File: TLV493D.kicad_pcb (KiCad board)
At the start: 2 copper layers, 11.7 x 22.6 mm, 10 parts, among them J1 Conn_01x04_Female, U1 TLV493D

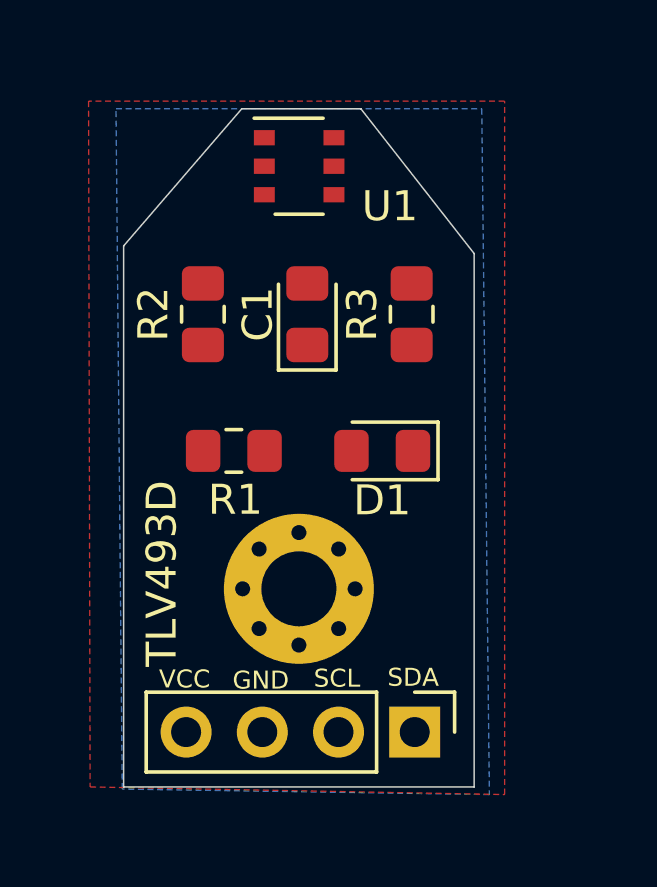
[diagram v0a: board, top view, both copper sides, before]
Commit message: Corrections routeo
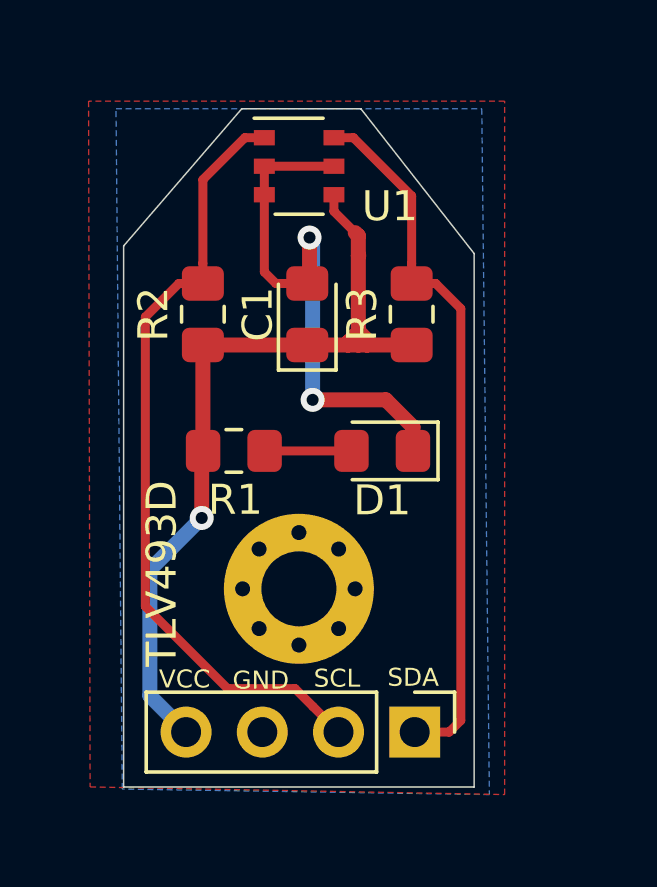
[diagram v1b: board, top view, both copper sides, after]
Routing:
- net VCC: track 0.00 -> 31.0 mm, vias 0 -> 1
- net /SCL: track 0.00 -> 26.3 mm
- net /SDA: track 0.00 -> 23.7 mm
- net GND: track 0.00 -> 19.0 mm, vias 0 -> 2
- net Net-(D1-Pad2): track 0.00 -> 2.90 mm
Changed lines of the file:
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@@
-(kicad_pcb (version 20171130) (host pcbnew "(5.1.4-0-10_14)")
+(kicad_pcb (version 20171130) (host pcbnew "(5.1.4)-1")
   (general
     (thickness 1.6)
     (drawings 15)
-    (tracks 0)
+    (tracks 61)
     (zones 0)
     (modules 10)
@@
     (34 B.Paste user)
     (35 F.Paste user)
-    (36 B.SilkS user)
+    (36 B.SilkS user hide)
     (37 F.SilkS user)
     (38 B.Mask user)
@@
   (gr_line (start 155.99 98.044) (end 159.766 102.87) (layer Edge.Cuts) (width 0.05))
   (gr_line (start 152.02 98.044) (end 155.99 98.044) (layer Edge.Cuts) (width 0.05))
+  (segment (start 152.7724 100.9092) (end 152.7724 103.4837) (width 0.3) (layer F.Cu) (net 1))
+  (segment (start 153.1567 103.868) (end 154.2034 103.868) (width 0.3) (layer F.Cu) (net 1))
+  (segment (start 152.7724 103.4837) (end 153.1567 103.868) (width 0.3) (layer F.Cu) (net 1))
+  (segment (start 152.7724 99.9592) (end 152.7724 100.9092) (width 0.3) (layer F.Cu) (net 1))
+  (segment (start 152.7724 99.9592) (end 155.0924 99.9592) (width 0.3) (layer F.Cu) (net 1))
+  (via (at 154.3812 107.7468) (size 0.8) (drill 0.4) (layers F.Cu B.Cu) (net 1))
+  (segment (start 156.8248 107.7468) (end 154.3812 107.7468) (width 0.5) (layer F.Cu) (net 1))
+  (segment (start 157.7266 109.4486) (end 157.7266 108.6486) (width 0.5) (layer F.Cu) (net 1))
+  (segment (start 157.7266 108.6486) (end 156.8248 107.7468) (width 0.5) (layer F.Cu) (net 1))
+  (via (at 154.2796 102.3366) (size 0.8) (drill 0.4) (layers F.Cu B.Cu) (net 1))
+  (segment (start 154.3812 107.7468) (end 154.3812 102.4382) (width 0.5) (layer B.Cu) (net 1))
+  (segment (start 154.3812 102.4382) (end 154.2796 102.3366) (width 0.5) (layer B.Cu) (net 1))
+  (segment (start 154.2796 103.7918) (end 154.2034 103.868) (width 0.5) (layer F.Cu) (net 1))
+  (segment (start 154.2796 102.3366) (end 154.2796 103.7918) (width 0.5) (layer F.Cu) (net 1))
+  (segment (start 150.7236 109.4412) (end 150.731 109.4486) (width 0.5) (layer F.Cu) (net 2))
+  (segment (start 150.7236 105.918) (end 150.7236 109.4412) (width 0.5) (layer F.Cu) (net 2))
+  (segment (start 150.7236 105.918) (end 154.2034 105.918) (width 0.5) (layer F.Cu) (net 2))
+  (segment (start 156.1973 105.918) (end 157.6832 105.918) (width 0.5) (layer F.Cu) (net 2))
+  (segment (start 154.2034 105.918) (end 155.5623 105.918) (width 0.5) (layer F.Cu) (net 2))
+  (segment (start 155.0924 100.9092) (end 155.0924 101.4642) (width 0.3) (layer F.Cu) (net 2))
+  (segment (start 155.5623 105.8291) (end 155.9198 105.4716) (width 0.5) (layer F.Cu) (net 2))
+  (segment (start 155.5623 105.918) (end 155.5623 105.8291) (width 0.5) (layer F.Cu) (net 2))
+  (segment (start 156.1973 105.7491) (end 155.9198 105.4716) (width 0.5) (layer F.Cu) (net 2))
+  (segment (start 156.1973 105.918) (end 156.1973 105.7491) (width 0.5) (layer F.Cu) (net 2))
+  (segment (start 155.9052 102.95) (end 155.9198 102.9354) (width 0.5) (layer F.Cu) (net 2))
+  (segment (start 155.9052 105.918) (end 155.9052 102.95) (width 0.5) (layer F.Cu) (net 2))
+  (segment (start 155.9198 102.2916) (end 155.9198 102.9354) (width 0.3) (layer F.Cu) (net 2))
+  (segment (start 155.9198 102.9354) (end 155.9198 105.4716) (width 0.3) (layer F.Cu) (net 2))
+  (segment (start 155.9052 105.918) (end 156.1973 105.918) (width 0.5) (layer F.Cu) (net 2))
+  (segment (start 155.5623 105.918) (end 155.9052 105.918) (width 0.5) (layer F.Cu) (net 2))
+  (segment (start 155.9052 102.277) (end 155.80165 102.17345) (width 0.5) (layer F.Cu) (net 2))
+  (segment (start 155.9052 102.95) (end 155.9052 102.277) (width 0.5) (layer F.Cu) (net 2))
+  (segment (start 155.0924 101.4642) (end 155.80165 102.17345) (width 0.3) (layer F.Cu) (net 2))
+  (segment (start 155.80165 102.17345) (end 155.9198 102.2916) (width 0.3) (layer F.Cu) (net 2))
+  (via (at 150.6855 111.6838) (size 0.8) (drill 0.4) (layers F.Cu B.Cu) (net 2))
+  (segment (start 150.6855 109.4941) (end 150.731 109.4486) (width 0.5) (layer F.Cu) (net 2))
+  (segment (start 150.6855 111.6838) (end 150.6855 109.4941) (width 0.5) (layer F.Cu) (net 2))
+  (segment (start 148.957 117.6134) (end 150.1648 118.8212) (width 0.5) (layer B.Cu) (net 2))
+  (segment (start 150.6855 111.6838) (end 148.957 113.4123) (width 0.5) (layer B.Cu) (net 2))
+  (segment (start 148.957 113.4123) (end 148.957 117.6134) (width 0.5) (layer B.Cu) (net 2))
+  (segment (start 152.781 109.4486) (end 155.6766 109.4486) (width 0.3) (layer F.Cu) (net 3))
+  (segment (start 150.7236 103.193) (end 150.7236 103.868) (width 0.3) (layer F.Cu) (net 4))
+  (segment (start 150.7236 100.408) (end 150.7236 103.193) (width 0.3) (layer F.Cu) (net 4))
+  (segment (start 152.1224 99.0092) (end 150.7236 100.408) (width 0.3) (layer F.Cu) (net 4))
+  (segment (start 152.7724 99.0092) (end 152.1224 99.0092) (width 0.3) (layer F.Cu) (net 4))
+  (segment (start 149.9236 103.868) (end 148.8059 104.9857) (width 0.3) (layer F.Cu) (net 4))
+  (segment (start 150.7236 103.868) (end 149.9236 103.868) (width 0.3) (layer F.Cu) (net 4))
+  (segment (start 148.8059 104.9857) (end 148.8059 114.6302) (width 0.3) (layer F.Cu) (net 4))
+  (segment (start 154.394801 117.971201) (end 155.2448 118.8212) (width 0.3) (layer F.Cu) (net 4))
+  (segment (start 153.794799 117.371199) (end 154.394801 117.971201) (width 0.3) (layer F.Cu) (net 4))
+  (segment (start 151.546899 117.371199) (end 153.794799 117.371199) (width 0.3) (layer F.Cu) (net 4))
+  (segment (start 148.8059 114.6302) (end 151.546899 117.371199) (width 0.3) (layer F.Cu) (net 4))
+  (segment (start 157.6832 103.193) (end 157.6832 103.868) (width 0.3) (layer F.Cu) (net 5))
+  (segment (start 157.6832 100.95) (end 157.6832 103.193) (width 0.3) (layer F.Cu) (net 5))
+  (segment (start 155.7424 99.0092) (end 157.6832 100.95) (width 0.3) (layer F.Cu) (net 5))
+  (segment (start 155.0924 99.0092) (end 155.7424 99.0092) (width 0.3) (layer F.Cu) (net 5))
+  (segment (start 158.9348 118.8212) (end 157.7848 118.8212) (width 0.3) (layer F.Cu) (net 5))
+  (segment (start 159.3215 118.4345) (end 158.9348 118.8212) (width 0.3) (layer F.Cu) (net 5))
+  (segment (start 159.3215 104.7063) (end 159.3215 118.4345) (width 0.3) (layer F.Cu) (net 5))
+  (segment (start 158.4832 103.868) (end 159.3215 104.7063) (width 0.3) (layer F.Cu) (net 5))
+  (segment (start 157.6832 103.868) (end 158.4832 103.868) (width 0.3) (layer F.Cu) (net 5))
   (zone (net 1) (net_name GND) (layer F.Cu) (hatch edge 0.508)
     (connect_pads (clearance 0.508))

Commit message: new sizes
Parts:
- added G***: LOGO, Aesthetics:SCL, F.Cu at (156.2, 116.2)
- added G***: LOGO, Aesthetics:3v3, F.Cu at (151.1, 116.1)
- added G***: LOGO, Aesthetics:GND, F.Cu at (153.7, 116.1)
- added G***: LOGO, Aesthetics:SDA, F.Cu at (158.8, 116.2)
- added G***: LOGO, Aesthetics:SDA, B.Cu at (158.8, 116.2)
- added G***: LOGO, Aesthetics:GND, B.Cu at (153.7, 116.5)
- added G***: LOGO, Aesthetics:3v3, B.Cu at (151.3, 116.2)
- added G***: LOGO, Aesthetics:SCL, B.Cu at (156.1, 116.2)
- moved D1 3.67 mm to (159.7, 111.5), turned to 270 degrees
- moved R1 2.86 mm to (150.6, 112.1), turned to 90 degrees
- moved REF** 2.55 mm to (155.0, 111.8)
- moved R3 1.96 mm to (159.6, 105.3)
- moved REF** 1.71 mm to (155.0, 106.5)
- moved G*** 1.18 mm to (155.1, 100.7)
- moved U1 1.12 mm to (155.1, 99.9)
- moved J1 1.02 mm to (158.8, 118.8)
- moved C1 0.91 mm to (155.0, 105.3)
- moved R2 0.58 mm to (150.7, 105.5)
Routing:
- net VCC: track 31.0 -> 0.00 mm, vias 1 -> 0
- net /SCL: track 26.3 -> 0.00 mm
- net /SDA: track 23.7 -> 0.00 mm
- net GND: track 19.0 -> 0.00 mm, vias 2 -> 0
- net Net-(D1-Pad2): track 2.90 -> 0.00 mm
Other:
- board size 11.7 x 22.6 mm -> 14 x 22.6 mm
- board text removed: "GND"
- board text removed: "SCL"
- board text removed: "SDA"
- board text removed: "VCC"

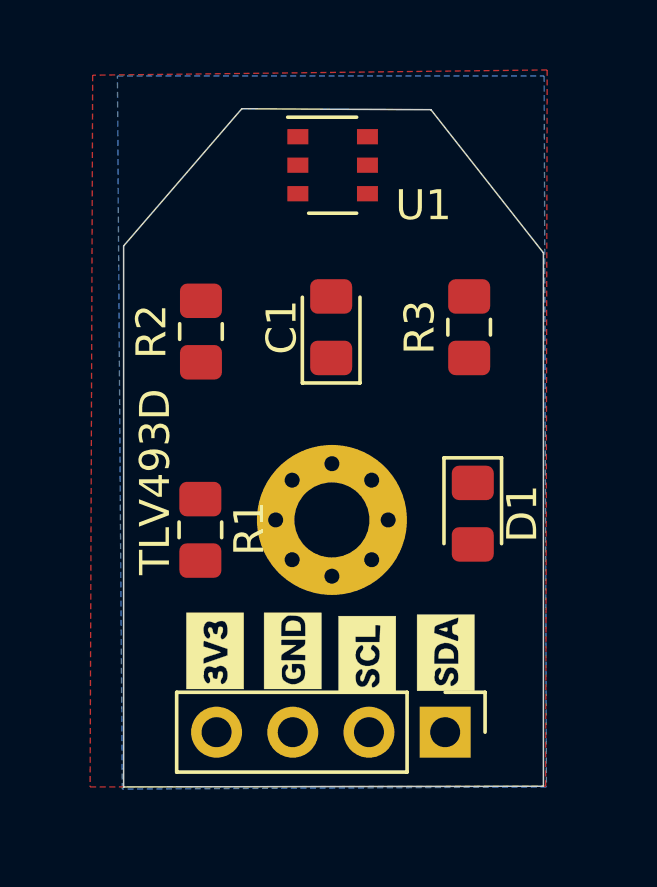
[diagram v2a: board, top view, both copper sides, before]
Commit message: fix countour
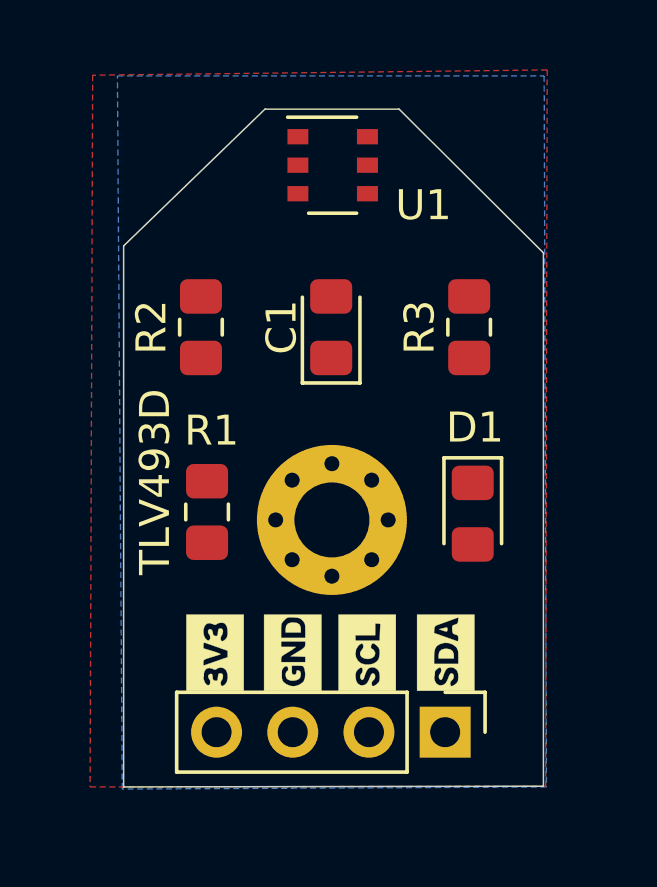
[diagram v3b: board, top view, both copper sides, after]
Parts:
- moved R1 0.64 mm to (150.9, 111.5)
- moved G*** 0.30 mm to (153.7, 116.2)
- moved R2 0.14 mm to (150.7, 105.3)
- moved G*** 0.08 mm to (158.8, 116.2)
- moved G*** 0.06 mm to (151.1, 116.2)
- moved G*** 0.06 mm to (153.7, 116.2)
- moved G*** 0.06 mm to (156.1, 116.2)
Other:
- outline, holes or cut-outs redrawn

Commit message: Fix logos
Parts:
- renumbered D1 to PWR
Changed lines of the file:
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@@
     (tags "LED handsolder")
     (attr smd)
-    (fp_text reference D1 (at -2.8661 -0.0714 180) (layer F.SilkS)
+    (fp_text reference PWR (at -2.8661 -0.0714 180) (layer F.SilkS)
       (effects (font (size 1 1) (thickness 0.15)))
     )
@@
     (arrow2b (pts (xy 148.127875 94.972805) (xy 149.255425 94.388398)))
   )
-  (gr_text v1.0 (at 157.988 114.046 90) (layer B.SilkS)
+  (gr_text v1.0 (at 151.0919 111.1504 90) (layer B.SilkS)
     (effects (font (size 1 1) (thickness 0.15)) (justify mirror))
   )
-  (gr_text TLV493D (at 149.352 113.538 90) (layer B.SilkS)
+  (gr_text TLV493D (at 149.1869 111.8362 90) (layer B.SilkS)
     (effects (font (size 1 1) (thickness 0.25)) (justify mirror))
   )

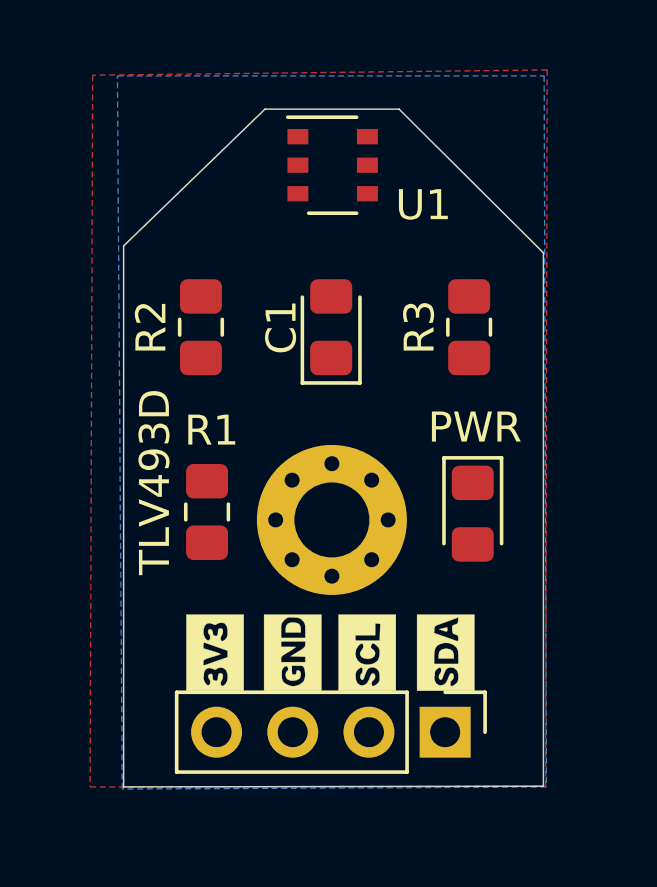
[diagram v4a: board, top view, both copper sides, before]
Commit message: Routeo witout GND
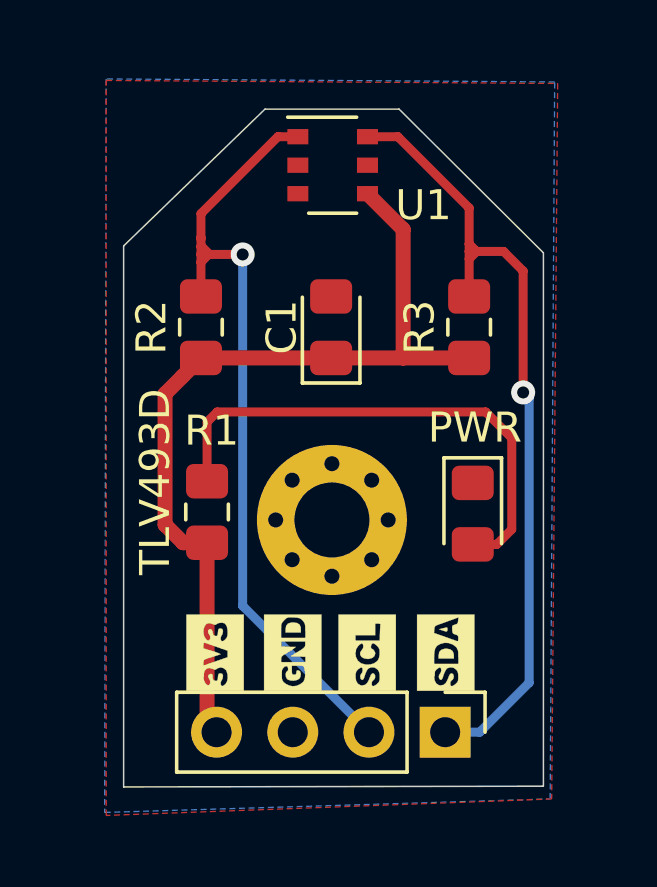
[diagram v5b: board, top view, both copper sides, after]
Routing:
- net VCC: track 0.00 -> 29.1 mm
- net /SDA: track 0.00 -> 27.4 mm, vias 0 -> 1
- net /SCL: track 0.00 -> 27.0 mm, vias 0 -> 1
- net Net-(D1-Pad2): track 0.00 -> 17.2 mm
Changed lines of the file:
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@@
     (thickness 1.6)
     (drawings 17)
-    (tracks 0)
+    (tracks 55)
     (zones 0)
     (modules 18)
@@
     (43 Eco2.User user)
     (44 Edge.Cuts user)
-    (45 Margin user)
+    (45 Margin user hide)
     (46 B.CrtYd user)
     (47 F.CrtYd user)
@@
   (gr_line (start 148.082 120.65) (end 162.075 120.625) (layer Edge.Cuts) (width 0.05))
   (gr_line (start 162.075 102.845) (end 162.075 120.625) (layer Edge.Cuts) (width 0.05))
+  (segment (start 150.8633 118.5083) (end 151.18 118.825) (width 0.5) (layer F.Cu) (net 2))
+  (segment (start 150.8633 112.5093) (end 150.8633 118.5083) (width 0.5) (layer F.Cu) (net 2))
+  (segment (start 150.66 106.35) (end 155 106.35) (width 0.5) (layer F.Cu) (net 2))
+  (segment (start 150.036628 106.973372) (end 150.66 106.35) (width 0.5) (layer F.Cu) (net 2))
+  (segment (start 149.46329 107.54671) (end 150.036628 106.973372) (width 0.5) (layer F.Cu) (net 2))
+  (segment (start 149.46329 111.90929) (end 149.46329 107.54671) (width 0.5) (layer F.Cu) (net 2))
+  (segment (start 150.0633 112.5093) (end 149.46329 111.90929) (width 0.5) (layer F.Cu) (net 2))
+  (segment (start 150.8633 112.5093) (end 150.0633 112.5093) (width 0.5) (layer F.Cu) (net 2))
+  (segment (start 157.4 102.065) (end 156.215001 100.880001) (width 0.5) (layer F.Cu) (net 2))
+  (segment (start 157.4 106.35) (end 157.4 102.065) (width 0.5) (layer F.Cu) (net 2))
+  (segment (start 159.6 106.35) (end 157.4 106.35) (width 0.5) (layer F.Cu) (net 2))
+  (segment (start 157.4 106.35) (end 155 106.35) (width 0.5) (layer F.Cu) (net 2))
+  (segment (start 159.72 112.565) (end 160.52 112.565) (width 0.3) (layer F.Cu) (net 3))
+  (segment (start 160.52 112.565) (end 161.02001 112.06499) (width 0.3) (layer F.Cu) (net 3))
+  (segment (start 161.02001 112.06499) (end 161.02001 109.02001) (width 0.3) (layer F.Cu) (net 3))
+  (segment (start 161.02001 109.02001) (end 160.15 108.15) (width 0.3) (layer F.Cu) (net 3))
+  (segment (start 160.15 108.15) (end 151.2 108.15) (width 0.3) (layer F.Cu) (net 3))
+  (segment (start 150.8633 108.4867) (end 150.8633 110.4593) (width 0.3) (layer F.Cu) (net 3))
+  (segment (start 151.2 108.15) (end 150.8633 108.4867) (width 0.3) (layer F.Cu) (net 3))
+  (segment (start 153.24 98.975) (end 153.89 98.975) (width 0.3) (layer F.Cu) (net 4))
+  (segment (start 153.225 98.975) (end 153.24 98.975) (width 0.3) (layer F.Cu) (net 4))
+  (segment (start 150.66 101.54) (end 153.225 98.975) (width 0.3) (layer F.Cu) (net 4))
+  (segment (start 150.66 102.34) (end 150.66 102.39) (width 0.3) (layer F.Cu) (net 4))
+  (segment (start 150.66 102.64) (end 150.66 102.34) (width 0.3) (layer F.Cu) (net 4))
+  (segment (start 150.66 102.34) (end 150.66 101.54) (width 0.3) (layer F.Cu) (net 4))
+  (segment (start 150.66 102.89) (end 150.66 102.64) (width 0.3) (layer F.Cu) (net 4))
+  (via (at 152.05 102.9) (size 0.8) (drill 0.4) (layers F.Cu B.Cu) (net 4))
+  (segment (start 156.26 118.825) (end 152.05 114.615) (width 0.3) (layer B.Cu) (net 4))
+  (segment (start 152.05 114.615) (end 152.05 102.9) (width 0.3) (layer B.Cu) (net 4))
+  (segment (start 150.67 102.9) (end 150.66 102.89) (width 0.3) (layer F.Cu) (net 4))
+  (segment (start 150.69 102.64) (end 150.95 102.9) (width 0.3) (layer F.Cu) (net 4))
+  (segment (start 150.66 102.64) (end 150.69 102.64) (width 0.3) (layer F.Cu) (net 4))
+  (segment (start 152.05 102.9) (end 150.95 102.9) (width 0.3) (layer F.Cu) (net 4))
+  (segment (start 150.95 102.9) (end 150.67 102.9) (width 0.3) (layer F.Cu) (net 4))
+  (segment (start 150.92 102.9) (end 150.66 103.16) (width 0.3) (layer F.Cu) (net 4))
+  (segment (start 150.95 102.9) (end 150.92 102.9) (width 0.3) (layer F.Cu) (net 4))
+  (segment (start 150.66 104.3) (end 150.66 103.16) (width 0.3) (layer F.Cu) (net 4))
+  (segment (start 150.66 103.16) (end 150.66 102.89) (width 0.3) (layer F.Cu) (net 4))
+  (segment (start 157.225 98.975) (end 156.21 98.975) (width 0.3) (layer F.Cu) (net 5))
+  (segment (start 159.6 101.35) (end 157.225 98.975) (width 0.3) (layer F.Cu) (net 5))
+  (segment (start 159.95 118.825) (end 161.6 117.175) (width 0.3) (layer B.Cu) (net 5))
+  (segment (start 158.8 118.825) (end 159.95 118.825) (width 0.3) (layer B.Cu) (net 5))
+  (via (at 161.4 107.5) (size 0.8) (drill 0.4) (layers F.Cu B.Cu) (net 5))
+  (segment (start 161.6 117.175) (end 161.6 107.7) (width 0.3) (layer B.Cu) (net 5))
+  (segment (start 161.6 107.7) (end 161.4 107.5) (width 0.3) (layer B.Cu) (net 5))
+  (segment (start 161.4 103.45) (end 160.75 102.8) (width 0.3) (layer F.Cu) (net 5))
+  (segment (start 159.85 102.8) (end 159.6 102.55) (width 0.3) (layer F.Cu) (net 5))
+  (segment (start 159.6 102.55) (end 159.6 101.35) (width 0.3) (layer F.Cu) (net 5))
+  (segment (start 159.6 102.8) (end 159.6 102.55) (width 0.3) (layer F.Cu) (net 5))
+  (segment (start 160.75 102.8) (end 159.85 102.8) (width 0.3) (layer F.Cu) (net 5))
+  (segment (start 159.85 102.8) (end 159.6 102.8) (width 0.3) (layer F.Cu) (net 5))
+  (segment (start 159.85 102.8) (end 159.6 103.05) (width 0.3) (layer F.Cu) (net 5))
+  (segment (start 159.6 104.3) (end 159.6 103.05) (width 0.3) (layer F.Cu) (net 5))
+  (segment (start 159.6 103.05) (end 159.6 102.8) (width 0.3) (layer F.Cu) (net 5))
+  (segment (start 161.4 107.5) (end 161.4 103.45) (width 0.3) (layer F.Cu) (net 5))
   (zone (net 1) (net_name GND) (layer F.Cu) (hatch edge 0.508)
     (connect_pads (clearance 0.508))
     (min_thickness 0.254)
-    (fill (arc_segments 32) (thermal_gap 0.508) (thermal_bridge_width 0.508))
+    (fill yes (arc_segments 32) (thermal_gap 0.508) (thermal_bridge_width 0.508))
     (polygon
       (pts
-        (xy 162.2 96.75) (xy 147.05 96.925) (xy 146.9644 120.65) (xy 162.15 120.625)
+        (xy 147.5 97.1) (xy 162.55 97.2) (xy 162.35 121.05) (xy 147.5 121.6)
       )
     )
@@
     (connect_pads (clearance 0.508))
     (min_thickness 0.254)
-    (fill (arc_segments 32) (thermal_gap 0.508) (thermal_bridge_width 0.508))
+    (fill yes (arc_segments 32) (thermal_gap 0.508) (thermal_bridge_width 0.508))
     (polygon
       (pts
-        (xy 147.875 96.95) (xy 162.1 96.95) (xy 162.175 120.65) (xy 148.036339 120.721183)
+        (xy 147.45 121.5) (xy 162.3 121.05) (xy 162.45 97.15) (xy 147.5 97.05)
       )
     )
